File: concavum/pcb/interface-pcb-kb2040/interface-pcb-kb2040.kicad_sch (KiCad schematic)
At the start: 9 parts, among them J1 Audio_Jack, J2 FPC_connector, U1 Adafruit_KB2040, U2 MCP23017_SO

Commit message: Replace elongated holes with ordinary ones
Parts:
- C1: footprint Capacitor_SMD:C_0603_1608Metric -> Capacitor_SMD:C_1206_3216Metric
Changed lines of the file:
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@@
       (effects (font (size 1.27 1.27)) (justify left))
     )
-    (property "Footprint" "Capacitor_SMD:C_0603_1608Metric" (id 2) (at 207.9752 102.87 0)
+    (property "Footprint" "Capacitor_SMD:C_1206_3216Metric" (id 2) (at 207.9752 102.87 0)
       (effects (font (size 1.27 1.27)) hide)
     )
@@
     )
     (path "/8afb3065-5901-4646-b749-d92eee19184b"
-      (reference "C1") (unit 1) (value "100n") (footprint "Capacitor_SMD:C_0603_1608Metric")
+      (reference "C1") (unit 1) (value "100n") (footprint "Capacitor_SMD:C_1206_3216Metric")
     )
     (path "/d385ebb9-fe43-4fe3-ae5a-b83665559f7f"

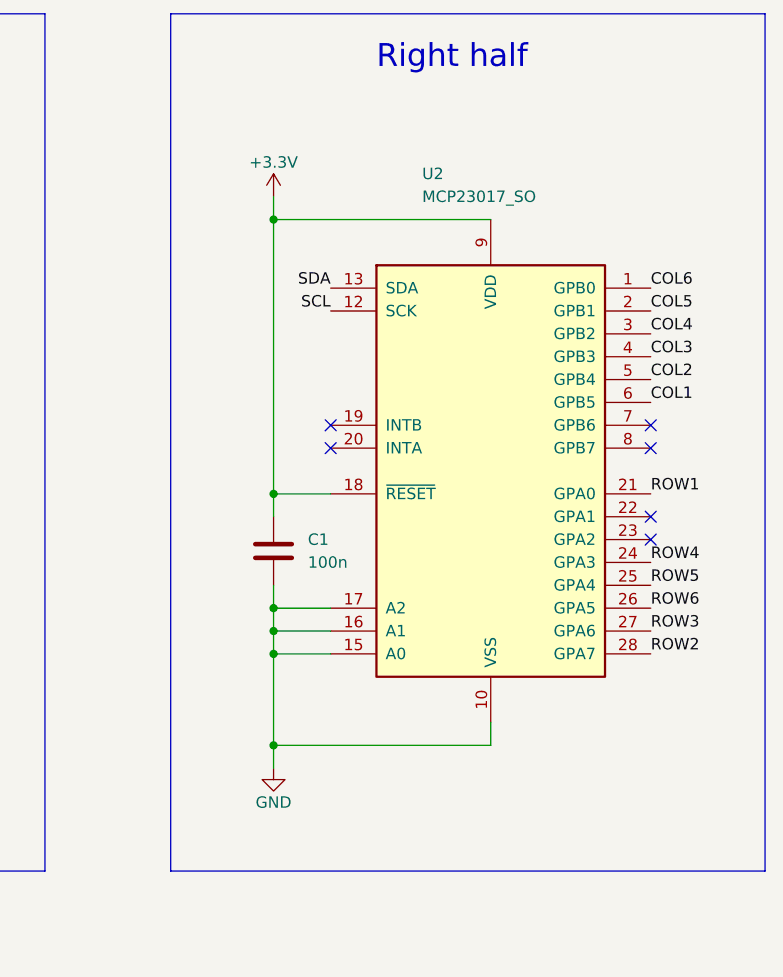
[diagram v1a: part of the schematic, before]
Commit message: Add option to use MCP23018 instead of MCP23017
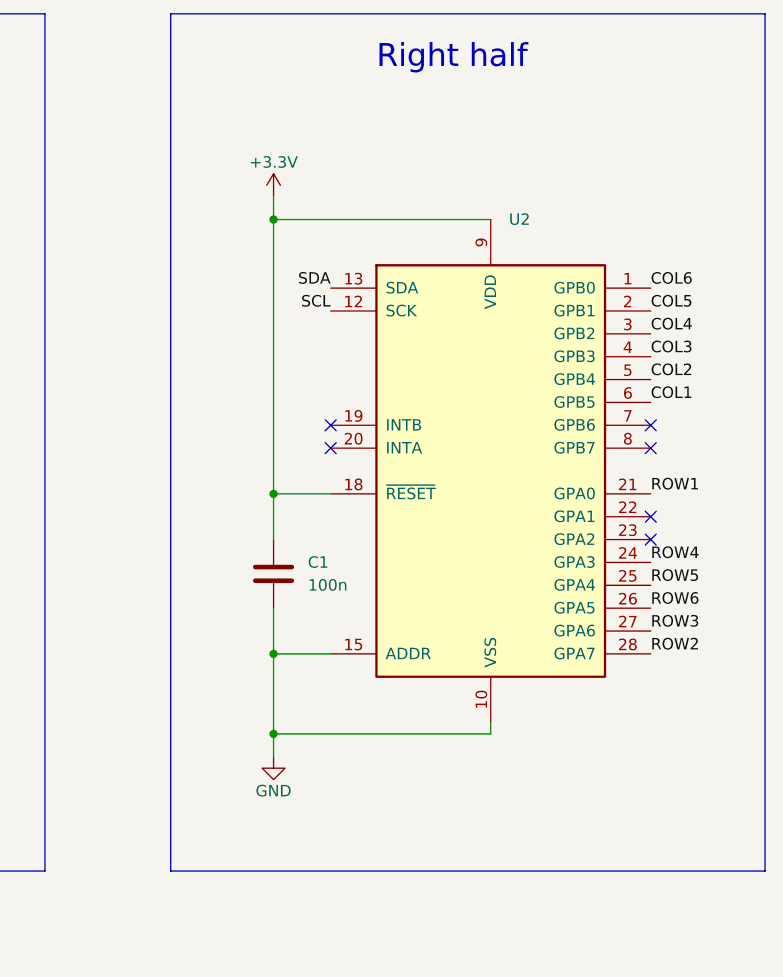
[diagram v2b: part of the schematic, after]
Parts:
- removed U2: MCP23017_SO, Package_SO:SOIC-28W_7.5x17.9mm_P1.27mm, symbol Interface_Expansion:MCP23017_SO
- added U2: (no value), symbol Custom:MCP23017/MCP23018
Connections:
- net +3V3: now also U2.18 (~{RESET}), U2.9 (VDD)
- net COL1: now also U2.6 (GPB5)
- net COL2: now also U2.5 (GPB4)
- net COL3: now also U2.4 (GPB3)
- net COL4: now also U2.3 (GPB2)
- net COL5: now also U2.2 (GPB1)
- net COL6: now also U2.1 (GPB0)
- net GND: now also U2.10 (VSS), U2.15 (ADDR)
- net ROW1: now also U2.21 (GPA0)
- net ROW2: now also U2.28 (GPA7)
- net ROW3: now also U2.27 (GPA6)
- net ROW4: now also U2.24 (GPA3)
- net ROW5: now also U2.25 (GPA4)
- net ROW6: now also U2.26 (GPA5)
- net SCL: now also U2.12 (SCK)
- net SDA: now also U2.13 (SDA)
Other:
- moved on the sheet: C1
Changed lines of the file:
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@@
   (junction (at 149.86 116.84) (diameter 0) (color 0 0 0 0)
   )
+  (junction (at 207.01 119.38) (diameter 0) (color 0 0 0 0)
+  )
   (junction (at 149.86 63.5) (diameter 0) (color 0 0 0 0)
   )
@@
   (junction (at 207.01 62.23) (diameter 0) (color 0 0 0 0)
   )
-  (junction (at 207.01 107.95) (diameter 0) (color 0 0 0 0)
-  )
   (junction (at 207.01 110.49) (diameter 0) (color 0 0 0 0)
-  )
-  (junction (at 207.01 120.65) (diameter 0) (color 0 0 0 0)
-  )
-  (junction (at 207.01 105.41) (diameter 0) (color 0 0 0 0)
   )
   (junction (at 207.01 92.71) (diameter 0) (color 0 0 0 0)
@@
     (stroke (width 0) (type default) (color 0 0 0 0))
   )
-  (wire (pts (xy 207.01 110.49) (xy 207.01 120.65))
+  (wire (pts (xy 207.01 110.49) (xy 207.01 119.38))
     (stroke (width 0) (type default) (color 0 0 0 0))
   )
@@
     (stroke (width 0) (type default) (color 0 0 0 0))
   )
-  (wire (pts (xy 207.01 123.19) (xy 207.01 120.65))
+  (wire (pts (xy 207.01 119.38) (xy 207.01 121.92))
     (stroke (width 0) (type default) (color 0 0 0 0))
   )
@@
     (stroke (width 0) (type default) (color 0 0 0 0))
   )
-  (wire (pts (xy 207.01 102.87) (xy 207.01 105.41))
-    (stroke (width 0) (type default) (color 0 0 0 0))
-  )
   (wire (pts (xy 121.92 82.55) (xy 129.54 82.55))
     (stroke (width 0) (type default) (color 0 0 0 0))
@@
     (stroke (width 0) (type default) (color 0 0 0 0))
   )
-  (wire (pts (xy 207.01 107.95) (xy 207.01 105.41))
-    (stroke (width 0) (type default) (color 0 0 0 0))
-  )
-  (wire (pts (xy 207.01 120.65) (xy 231.14 120.65))
+  (wire (pts (xy 207.01 119.38) (xy 231.14 119.38))
     (stroke (width 0) (type default) (color 0 0 0 0))
   )
@@
     (stroke (width 0) (type default) (color 0 0 0 0))
   )
-  (wire (pts (xy 207.01 92.71) (xy 207.01 95.25))
+  (wire (pts (xy 207.01 92.71) (xy 207.01 97.79))
     (stroke (width 0) (type default) (color 0 0 0 0))
   )
@@
     (stroke (width 0) (type default) (color 0 0 0 0))
   )
-  (wire (pts (xy 231.14 118.11) (xy 231.14 120.65))
+  (wire (pts (xy 231.14 118.11) (xy 231.14 119.38))
     (stroke (width 0) (type default) (color 0 0 0 0))
   )
@@
     (stroke (width 0) (type default) (color 0 0 0 0))
   )
-  (wire (pts (xy 207.01 107.95) (xy 213.36 107.95))
-    (stroke (width 0) (type default) (color 0 0 0 0))
-  )
   (polyline (pts (xy 99.06 39.37) (xy 35.56 39.37))
     (stroke (width 0) (type default) (color 0 0 0 0))
@@
     (stroke (width 0) (type default) (color 0 0 0 0))
   )
-  (wire (pts (xy 207.01 105.41) (xy 213.36 105.41))
-    (stroke (width 0) (type default) (color 0 0 0 0))
-  )
   (wire (pts (xy 124.46 63.5) (xy 124.46 66.04))
     (stroke (width 0) (type default) (color 0 0 0 0))
@@
     (stroke (width 0) (type default) (color 0 0 0 0))
   )
-  (wire (pts (xy 207.01 110.49) (xy 207.01 107.95))
+  (wire (pts (xy 207.01 105.41) (xy 207.01 110.49))
     (stroke (width 0) (type default) (color 0 0 0 0))
   )
@@
     (pin "1")
   )
-  (symbol (lib_id "Interface_Expansion:MCP23017_SO") (at 231.14 90.17 0) (unit 1)
-    (in_bom yes) (on_board yes)
-    (property "Reference" "U2" (id 0) (at 223.52 57.15 0)
-      (effects (font (size 1.27 1.27)) (justify left))
-    )
-    (property "Value" "MCP23017_SO" (id 1) (at 223.52 59.69 0)
-      (effects (font (size 1.27 1.27)) (justify left))
-    )
-    (property "Footprint" "Package_SO:SOIC-28W_7.5x17.9mm_P1.27mm" (id 2) (at 236.22 115.57 0)
-      (effects (font (size 1.27 1.27)) (justify left) hide)
-    )
-    (property "Datasheet" "http://ww1.microchip.com/downloads/en/DeviceDoc/20001952C.pdf" (id 3) (at 236.22 118.11 0)
-      (effects (font (size 1.27 1.27)) (justify left) hide)
-    )
-    (pin "1")
-    (pin "10")
-    (pin "11")
-    (pin "12")
-    (pin "13")
-    (pin "14")
-    (pin "15")
-    (pin "16")
-    (pin "17")
-    (pin "18")
-    (pin "19")
-    (pin "2")
-    (pin "20")
-    (pin "21")
-    (pin "22")
-    (pin "23")
-    (pin "24")
-    (pin "25")
-    (pin "26")
-    (pin "27")
-    (pin "28")
-    (pin "3")
-    (pin "4")
-    (pin "5")
-    (pin "6")
-    (pin "7")
-    (pin "8")
-    (pin "9")
-  )
   (symbol (lib_id "power:+3.3V") (at 149.86 60.96 0) (unit 1)
     (in_bom yes) (on_board yes)
@@
     (pin "TN")
   )
-  (symbol (lib_id "Device:C") (at 207.01 99.06 0) (unit 1)
+  (symbol (lib_id "Device:C") (at 207.01 101.6 0) (unit 1)
     (in_bom yes) (on_board yes) (fields_autoplaced)
-    (property "Reference" "C1" (id 0) (at 210.82 97.7899 0)
-      (effects (font (size 1.27 1.27)) (justify left))
-    )
-    (property "Value" "100n" (id 1) (at 210.82 100.3299 0)
-      (effects (font (size 1.27 1.27)) (justify left))
-    )
-    (property "Footprint" "Capacitor_SMD:C_1206_3216Metric" (id 2) (at 207.9752 102.87 0)
-      (effects (font (size 1.27 1.27)) hide)
-    )
-    (property "Datasheet" "~" (id 3) (at 207.01 99.06 0)
+    (property "Reference" "C1" (id 0) (at 210.82 100.3299 0)
+      (effects (font (size 1.27 1.27)) (justify left))
+    )
+    (property "Value" "100n" (id 1) (at 210.82 102.8699 0)
+      (effects (font (size 1.27 1.27)) (justify left))
+    )
+    (property "Footprint" "Capacitor_SMD:C_1206_3216Metric" (id 2) (at 207.9752 105.41 0)
+      (effects (font (size 1.27 1.27)) hide)
+    )
+    (property "Datasheet" "~" (id 3) (at 207.01 101.6 0)
       (effects (font (size 1.27 1.27)) hide)
     )
@@
     (pin "1")
   )
-  (symbol (lib_id "power:GND") (at 207.01 123.19 0) (unit 1)
-    (in_bom yes) (on_board yes)
-    (property "Reference" "#PWR06" (id 0) (at 207.01 129.54 0)
-      (effects (font (size 1.27 1.27)) hide)
-    )
-    (property "Value" "GND" (id 1) (at 207.01 127 0))
-    (property "Footprint" "" (id 2) (at 207.01 123.19 0)
-      (effects (font (size 1.27 1.27)) hide)
-    )
-    (property "Datasheet" "" (id 3) (at 207.01 123.19 0)
+  (symbol (lib_id "power:GND") (at 207.01 121.92 0) (unit 1)
+    (in_bom yes) (on_board yes)
+    (property "Reference" "#PWR06" (id 0) (at 207.01 128.27 0)
+      (effects (font (size 1.27 1.27)) hide)
+    )
+    (property "Value" "GND" (id 1) (at 207.01 125.73 0))
+    (property "Footprint" "" (id 2) (at 207.01 121.92 0)
+      (effects (font (size 1.27 1.27)) hide)
+    )
+    (property "Datasheet" "" (id 3) (at 207.01 121.92 0)
       (effects (font (size 1.27 1.27)) hide)
     )
@@
     (pin "9")
   )
+  (symbol (lib_id "Custom:MCP23017{slash}MCP23018") (at 231.14 90.17 0) (unit 1)
+    (in_bom yes) (on_board yes) (fields_autoplaced)
+    (property "Reference" "U2" (id 0) (at 233.1594 62.23 0)
+      (effects (font (size 1.27 1.27)) (justify left))
+    )
+    (property "Value" "" (id 1) (at 233.1594 64.77 0)
+      (effects (font (size 1.27 1.27)) (justify left))
+    )
+    (property "Footprint" "" (id 2) (at 236.22 118.11 0)
+      (effects (font (size 1.27 1.27)) (justify left) hide)
+    )
+    (property "Datasheet" "http://ww1.microchip.com/downloads/en/DeviceDoc/20001952C.pdf" (id 3) (at 236.22 120.65 0)
+      (effects (font (size 1.27 1.27)) (justify left) hide)
+    )
+    (pin "1")
+    (pin "10")
+    (pin "11")
+    (pin "12")
+    (pin "13")
+    (pin "14")
+    (pin "15")
+    (pin "16")
+    (pin "17")
+    (pin "18")
+    (pin "19")
+    (pin "2")
+    (pin "20")
+    (pin "21")
+    (pin "22")
+    (pin "23")
+    (pin "24")
+    (pin "25")
+    (pin "26")
+    (pin "27")
+    (pin "28")
+    (pin "29")
+    (pin "3")
+    (pin "30")
+    (pin "4")
+    (pin "5")
+    (pin "6")
+    (pin "7")
+    (pin "8")
+    (pin "9")
+  )
   (symbol (lib_id "power:+3.3V") (at 77.47 59.69 0) (unit 1)
     (in_bom yes) (on_board yes)
@@
       (reference "U1") (unit 1) (value "Adafruit_KB2040") (footprint "Custom:Adafruit_KB2040")
     )
-    (path "/48cffc50-fb06-4eb1-9b93-78f85a43b110"
-      (reference "U2") (unit 1) (value "MCP23017_SO") (footprint "Package_SO:SOIC-28W_7.5x17.9mm_P1.27mm")
-    )
-  )
+    (path "/dcd54fce-75b2-413d-a029-34676a7040bd"
+      (reference "U2") (unit 1) (value "MCP23017/MCP23018") (footprint "Custom:MCP23017_SO_MCP23018_SO")
+    )
+  )

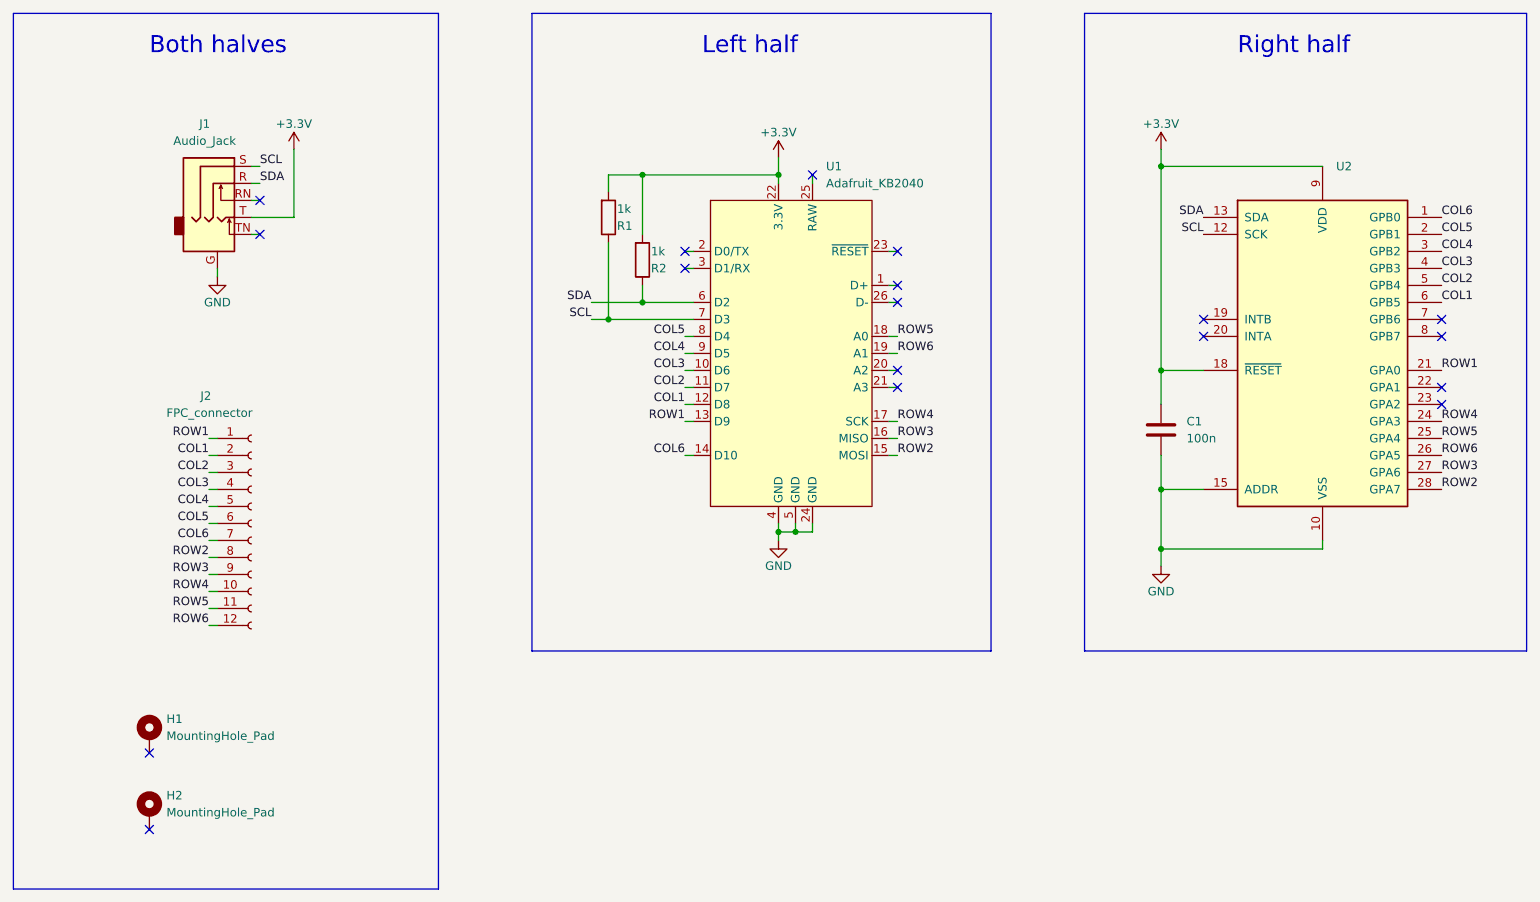
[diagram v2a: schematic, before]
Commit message: Change FPC connector pinout to increase clearances
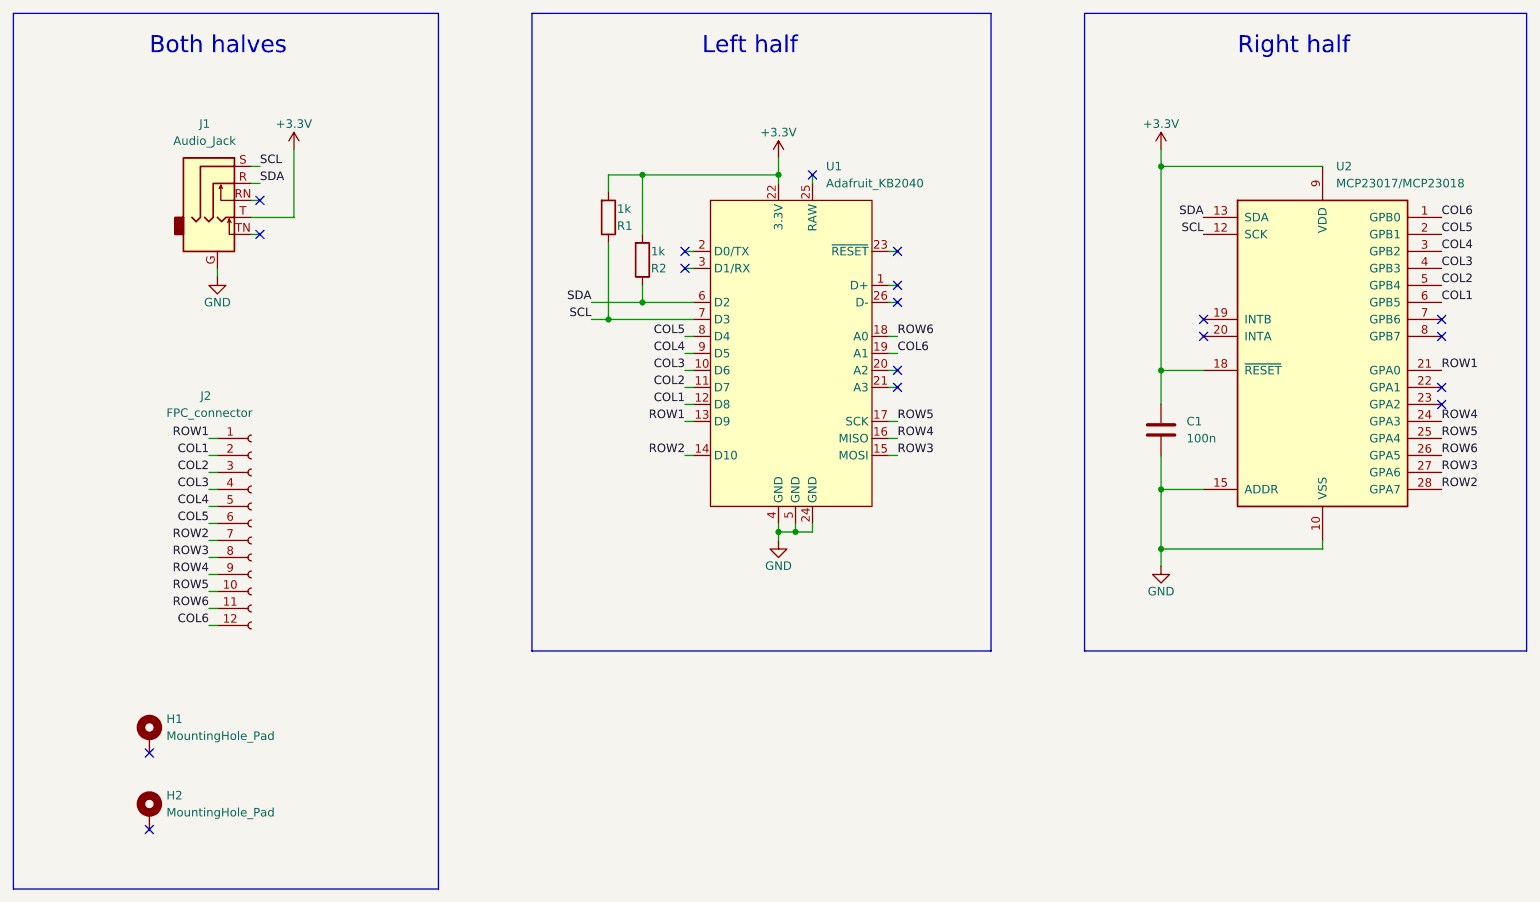
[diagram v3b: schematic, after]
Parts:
- U2: value (none) -> MCP23017/MCP23018; footprint (none) -> Custom:MCP23017_SO_MCP23018_SO
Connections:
- net COL6: now also J2.12 (Pin_12), U1.19 (A1); no longer J2.7 (Pin_7), U1.14 (D10)
- net ROW2: now also J2.7 (Pin_7), U1.14 (D10); no longer J2.8 (Pin_8), U1.15 (MOSI)
- net ROW3: now also J2.8 (Pin_8), U1.15 (MOSI); no longer J2.9 (Pin_9), U1.16 (MISO)
- net ROW4: now also J2.9 (Pin_9), U1.16 (MISO); no longer J2.10 (Pin_10), U1.17 (SCK)
- net ROW5: now also J2.10 (Pin_10), U1.17 (SCK); no longer J2.11 (Pin_11), U1.18 (A0)
- net ROW6: now also J2.11 (Pin_11), U1.18 (A0); no longer J2.12 (Pin_12), U1.19 (A1)
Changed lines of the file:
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@@
     (effects (font (size 1.27 1.27)) (justify left bottom))
   )
-  (label "ROW3" (at 64.77 123.19 180)
-    (effects (font (size 1.27 1.27)) (justify right bottom))
-  )
-  (label "COL6" (at 135.89 105.41 180)
-    (effects (font (size 1.27 1.27)) (justify right bottom))
+  (label "ROW3" (at 64.77 120.65 180)
+    (effects (font (size 1.27 1.27)) (justify right bottom))
+  )
+  (label "COL6" (at 167.64 90.17 0)
+    (effects (font (size 1.27 1.27)) (justify left bottom))
   )
   (label "SCL" (at 121.92 85.09 180)
@@
     (effects (font (size 1.27 1.27)) (justify right bottom))
   )
-  (label "COL6" (at 64.77 118.11 180)
+  (label "COL6" (at 64.77 130.81 180)
     (effects (font (size 1.27 1.27)) (justify right bottom))
   )
@@
     (effects (font (size 1.27 1.27)) (justify left bottom))
   )
-  (label "ROW6" (at 64.77 130.81 180)
-    (effects (font (size 1.27 1.27)) (justify right bottom))
-  )
-  (label "ROW5" (at 167.64 87.63 0)
+  (label "ROW6" (at 64.77 128.27 180)
+    (effects (font (size 1.27 1.27)) (justify right bottom))
+  )
+  (label "ROW5" (at 167.64 100.33 0)
     (effects (font (size 1.27 1.27)) (justify left bottom))
   )
@@
     (effects (font (size 1.27 1.27)) (justify left bottom))
   )
-  (label "ROW2" (at 64.77 120.65 180)
+  (label "ROW2" (at 64.77 118.11 180)
     (effects (font (size 1.27 1.27)) (justify right bottom))
   )
@@
     (effects (font (size 1.27 1.27)) (justify right bottom))
   )
-  (label "ROW5" (at 64.77 128.27 180)
+  (label "ROW5" (at 64.77 125.73 180)
     (effects (font (size 1.27 1.27)) (justify right bottom))
   )
@@
     (effects (font (size 1.27 1.27)) (justify left bottom))
   )
-  (label "ROW3" (at 167.64 102.87 0)
+  (label "ROW3" (at 167.64 105.41 0)
     (effects (font (size 1.27 1.27)) (justify left bottom))
   )
@@
     (effects (font (size 1.27 1.27)) (justify left bottom))
   )
-  (label "ROW6" (at 167.64 90.17 0)
+  (label "ROW6" (at 167.64 87.63 0)
     (effects (font (size 1.27 1.27)) (justify left bottom))
   )
@@
     (effects (font (size 1.27 1.27)) (justify right bottom))
   )
-  (label "ROW4" (at 64.77 125.73 180)
-    (effects (font (size 1.27 1.27)) (justify right bottom))
-  )
-  (label "ROW4" (at 167.64 100.33 0)
+  (label "ROW4" (at 64.77 123.19 180)
+    (effects (font (size 1.27 1.27)) (justify right bottom))
+  )
+  (label "ROW4" (at 167.64 102.87 0)
     (effects (font (size 1.27 1.27)) (justify left bottom))
   )
@@
     (effects (font (size 1.27 1.27)) (justify left bottom))
   )
-  (label "ROW2" (at 167.64 105.41 0)
-    (effects (font (size 1.27 1.27)) (justify left bottom))
+  (label "ROW2" (at 135.89 105.41 180)
+    (effects (font (size 1.27 1.27)) (justify right bottom))
   )
   (label "SCL" (at 72.39 62.23 0)
@@
       (effects (font (size 1.27 1.27)) (justify left))
     )
-    (property "Value" "" (id 1) (at 233.1594 64.77 0)
-      (effects (font (size 1.27 1.27)) (justify left))
-    )
-    (property "Footprint" "" (id 2) (at 236.22 118.11 0)
+    (property "Value" "MCP23017/MCP23018" (id 1) (at 233.1594 64.77 0)
+      (effects (font (size 1.27 1.27)) (justify left))
+    )
+    (property "Footprint" "Custom:MCP23017_SO_MCP23018_SO" (id 2) (at 236.22 118.11 0)
       (effects (font (size 1.27 1.27)) (justify left) hide)
     )
